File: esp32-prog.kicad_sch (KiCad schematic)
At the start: 43 parts, among them J1 USB_B_Micro_10118194-0001LF, J2 1.27mm_50mils_male_DW127R-22-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, Q1 AO3400A, Q2 AO3400A, SW1 SW_DIP_x02_50mil_1.27mm_TP-02, U1 AMS1117-3.3, U2 SRV05-4, U3 CH340C, U4 74LVC1G125GW_Nexperia, U5 74LVC1G125GW_Nexperia, U6 74LVC1G125GW_Nexperia, U7 74LVC1G125GW_Nexperia

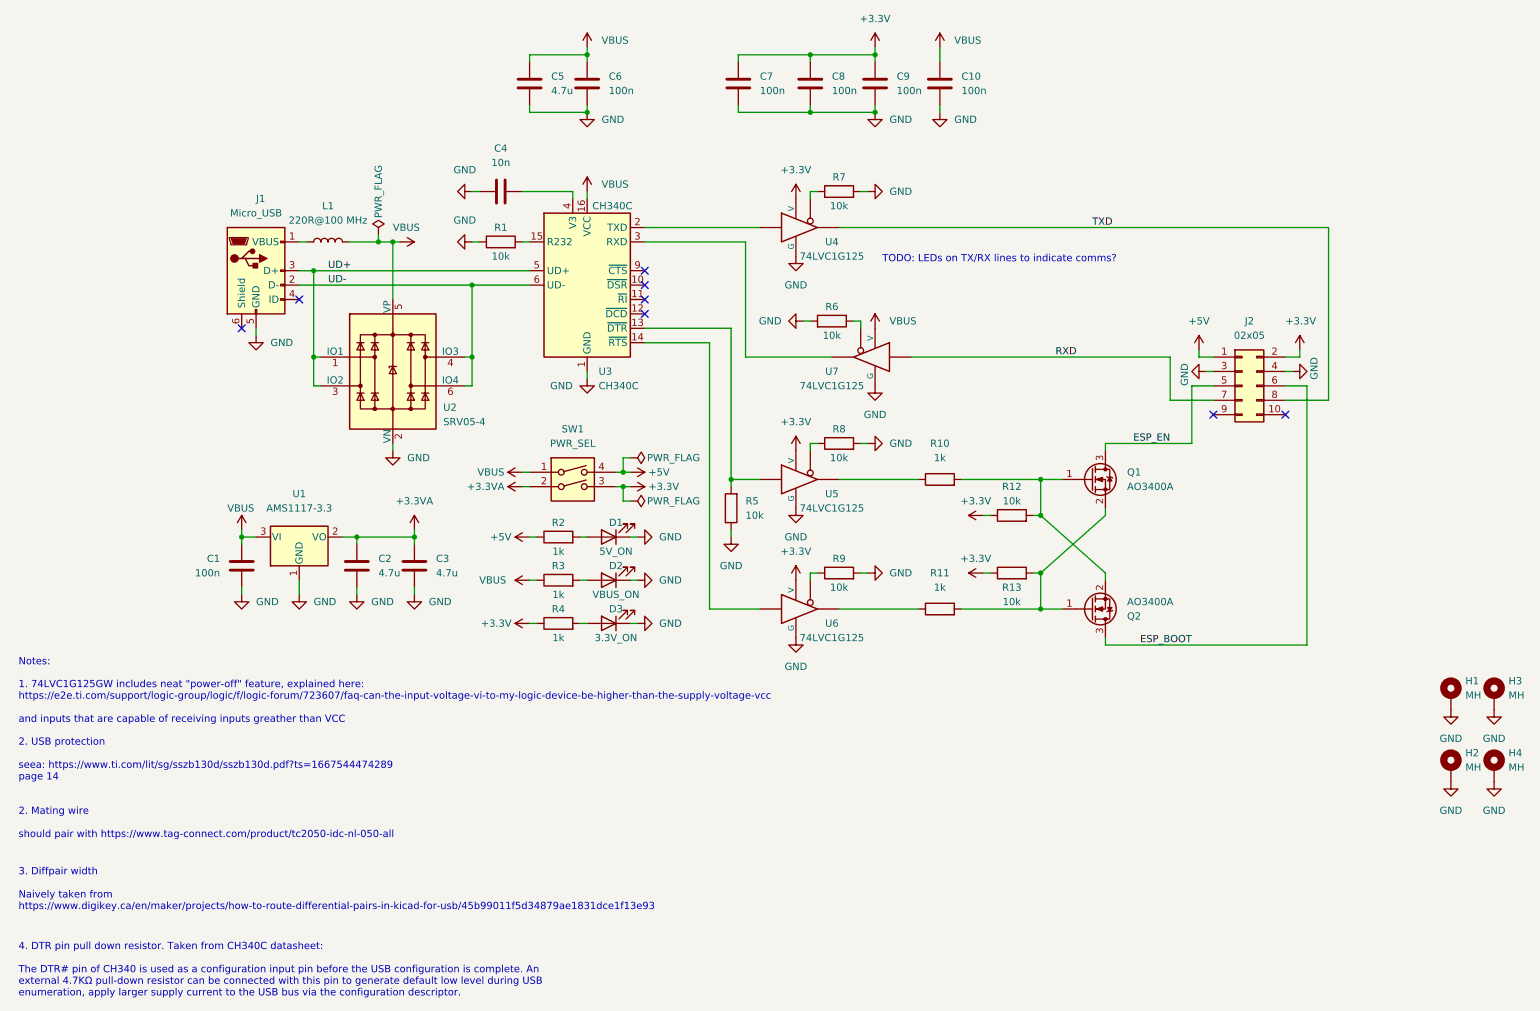
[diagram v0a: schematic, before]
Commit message: pcb: next revision schematics and prelim routing
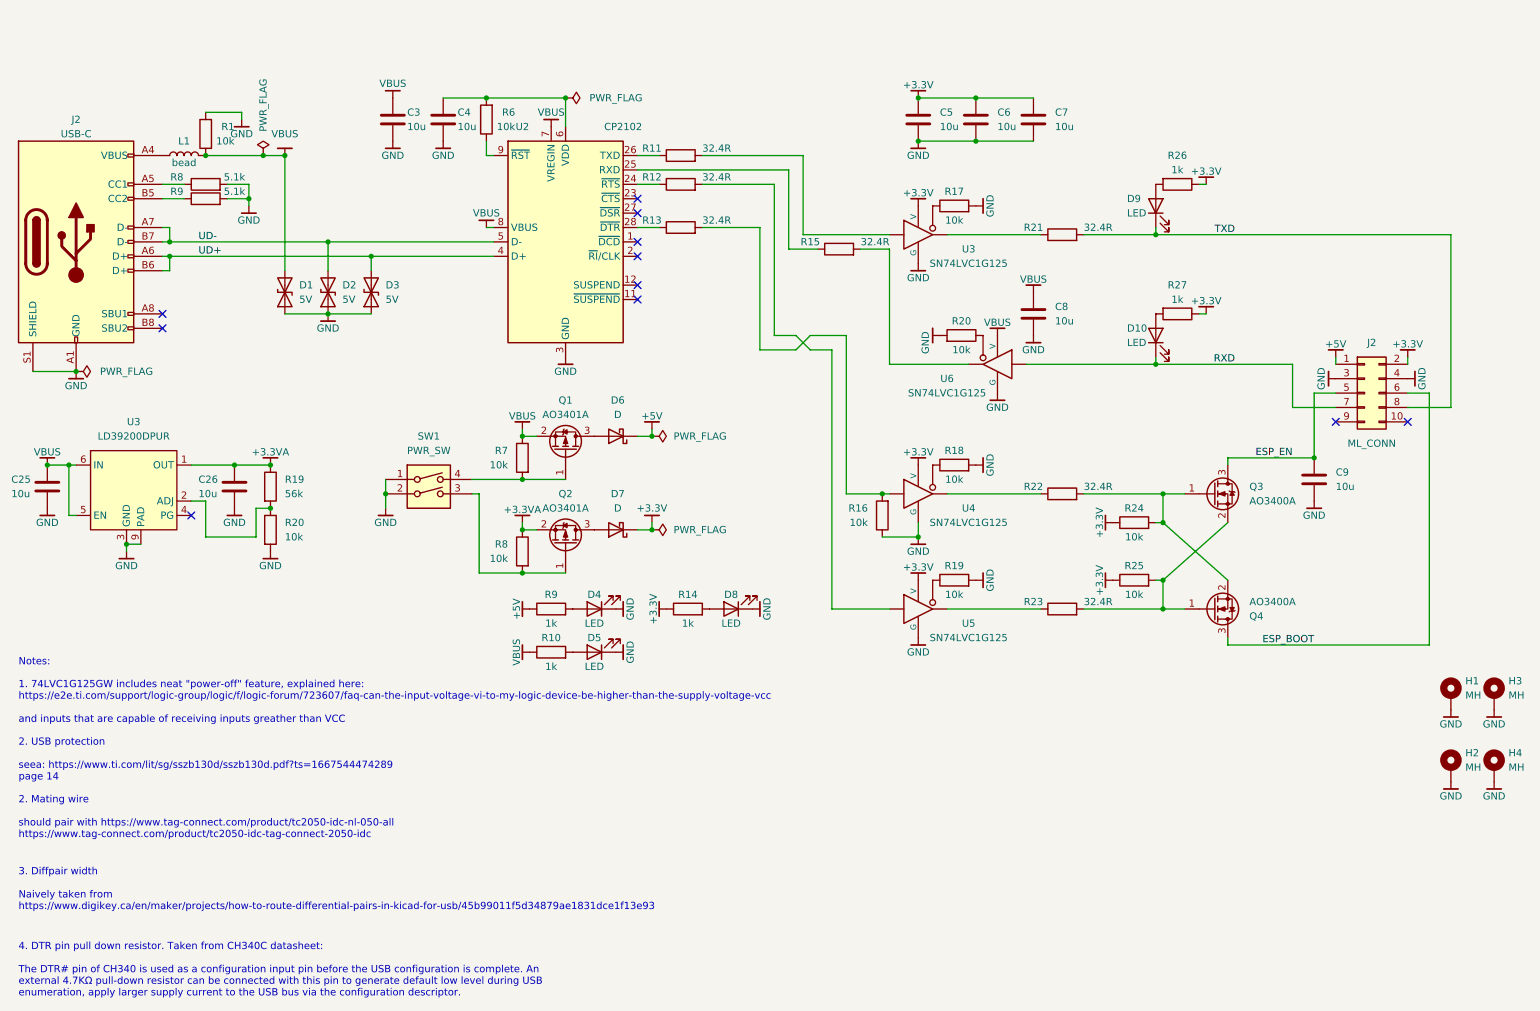
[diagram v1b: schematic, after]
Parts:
- removed C1, C6: 100n_0402_CL05B104KB54PNC, Capacitor_SMD:C_0603_1608Metric, symbol 00-kiml-capacitors-smd:100n_0402_CL05B104KB54PNC
- removed C2, C3, C5: 4.7u_1206_1206B475K500NT, Capacitor_SMD:C_1206_3216Metric, symbol 00-kiml-capacitors-smd:4.7u_1206_1206B475K500NT
- removed C4: 10n_0402_CL05B103KB5NNNC, Capacitor_SMD:C_0603_1608Metric, symbol 00-kiml-capacitors-smd:10n_0402_CL05B103KB5NNNC
- removed J1: USB_B_Micro_10118194-0001LF, 00-kiml-connector-usb:USB_Micro-B_Amphenol_10118194_Horizontal, symbol 00-kiml-connector:USB_B_Micro_10118194-0001LF
- removed J2: 1.27mm_50mils_male_DW127R-22-10-23_02x05, Connector_PinHeader_1.27mm:PinHeader_2x05_P1.27mm_Vertical, symbol 00-kiml-connector-pin-header-1.27mm:1.27mm_50mils_male_DW127R-22-10-23_02x05
- removed L1: 0805_FB_220R@100MHz_BLM21PG221SN1D, Inductor_SMD:L_0805_2012Metric_Pad1.15x1.40mm_HandSolder, symbol 00-kiml-inductors:0805_FB_220R@100MHz_BLM21PG221SN1D
- removed R10, R11: 1k_0402_0402WGF1001TCE, Resistor_SMD:R_0402_1005Metric, symbol 00-kiml-resistors-smd:1k_0402_0402WGF1001TCE
- removed U1: AMS1117-3.3, Package_TO_SOT_SMD:SOT-223-3_TabPin2, symbol 00-kiml-regulator-linear:AMS1117-3.3
- removed U2: SRV05-4, Package_TO_SOT_SMD:SOT-23-6, symbol 00-kiml-power-protection:SRV05-4
- removed U3: CH340C, Package_SO:SOIC-16_3.9x9.9mm_P1.27mm, symbol 00-kiml-interface_usb:CH340C
- removed U4, U5, U6, U7: 74LVC1G125GW_Nexperia, Package_TO_SOT_SMD:SOT-353_SC-70-5, symbol 00-kiml-74xGxx:74LVC1G125GW_Nexperia
- added C25, C26, C3, C4, C9: 10u_0402_LDK105CBJ106MVLF, Capacitor_SMD:C_0402_1005Metric, symbol 00-kiml-capacitors-smd:10u_0402_LDK105CBJ106MVLF
- added D1, D2, D3: SOD-882_0402_RCLAMP0521P-N, Diode_SMD:D_0402_1005Metric, symbol 00-kiml-power-protection:SOD-882_0402_RCLAMP0521P-N
- added D10, D9: 0402_BLUE_NCD0402B1, LED_SMD:LED_0402_1005Metric, symbol 00-kiml-led-smd:0402_BLUE_NCD0402B1
- added D6, D7: SS34, 00-kiml-diode:DO-214AC, symbol 00-kiml-diode:SS34
- added J2: TYPE-C-31-M-12, 00-kiml-connector-usb:USB_C_Receptacle_HRO_TYPE-C-31-M-12, symbol 00-kiml-connector-usb:USB_C_Receptacle_USB2.0_TYPE-C-31-M-12
- added J2: Conn-02x05_PZ254-2-05-Z-8.5, Connector_PinHeader_2.54mm:PinHeader_2x05_P2.54mm_Vertical, symbol 00-kiml-connector-pin-header-2.54mm:Conn-02x05_PZ254-2-05-Z-8.5
- added L1: FB_2A_0805_220R@100MHz_BLM21PG221SN1D, Inductor_SMD:L_0805_2012Metric_Pad1.15x1.40mm_HandSolder, symbol 00-kiml-inductors:FB_2A_0805_220R@100MHz_BLM21PG221SN1D
- added Q1, Q2: AO3401A, Package_TO_SOT_SMD:SOT-23, symbol 00-kiml-transistor-fet:AO3401A
- added R11, R12, R13, R15, R21, R22, R23: 32.4R_0402_AC0402FR-0732R4L, Resistor_SMD:R_0402_1005Metric, symbol 00-kiml-resistors-smd:32.4R_0402_AC0402FR-0732R4L
- added R19: 56k_0402_ERJ2RKF5602X, Resistor_SMD:R_0402_1005Metric, symbol 00-kiml-resistors-smd:56k_0402_ERJ2RKF5602X
- added R20, R6, R7, R8: 10k_0402_0402WGF1002TCE, Resistor_SMD:R_0402_1005Metric, symbol 00-kiml-resistors-smd:10k_0402_0402WGF1002TCE
- added R26, R27: 1k_0402_0402WGF1001TCE, Resistor_SMD:R_0402_1005Metric, symbol 00-kiml-resistors-smd:1k_0402_0402WGF1001TCE
- added R8, R9: 5.1k_0603_0603WAF5101T5E, Resistor_SMD:R_0603_1608Metric, symbol 00-kiml-resistors-smd:5.1k_0603_0603WAF5101T5E
- added U2: CP2102-GMR, Package_DFN_QFN:QFN-28-1EP_5x5mm_P0.5mm_EP3.35x3.35mm, symbol 00-kiml-interface_usb:CP2102-GMR
- added U3: LD39200DPUR, Package_DFN_QFN:DFN-8-1EP_4x4mm_P0.8mm_EP2.3x3.24mm, symbol 00-kiml-regulator-linear:LD39200DPUR
- added U3, U4, U5, U6: TI_SN74LVC1G125DRYR, Package_SON:Texas_USON-6_1x1.45mm_P0.5mm_SMD, symbol 00-kiml-74xGxx:TI_SN74LVC1G125DRYR
- C5: renamed from C7; value 100n_0402_CL05B104KB54PNC -> 10u_0402_LDK105CBJ106MVLF; footprint Capacitor_SMD:C_0603_1608Metric -> Capacitor_SMD:C_0402_1005Metric; symbol 00-kiml-capacitors-smd:100n_0402_CL05B104KB54PNC -> 00-kiml-capacitors-smd:10u_0402_LDK105CBJ106MVLF; LNK1 https://jlcpcb.com/partdetail/291005-CL05B104KB54PNC/C307331 -> https://jlcpcb.com/partdetail/TaiyoYuden-LDK105CBJ106MVLF/C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; MFR Samsung -> Taiyo; MPN CL05B104KB54PNC -> LDK105CBJ106MVLF; Rating 50V -> 10V; SNB1 Basic part -> Extended Part; SPN1 C307331 -> C386033; Tolerance 10% -> (none); UserValue 100n -> 10u
- C6: renamed from C8; value 100n_0402_CL05B104KB54PNC -> 10u_0402_LDK105CBJ106MVLF; footprint Capacitor_SMD:C_0603_1608Metric -> Capacitor_SMD:C_0402_1005Metric; symbol 00-kiml-capacitors-smd:100n_0402_CL05B104KB54PNC -> 00-kiml-capacitors-smd:10u_0402_LDK105CBJ106MVLF; LNK1 https://jlcpcb.com/partdetail/291005-CL05B104KB54PNC/C307331 -> https://jlcpcb.com/partdetail/TaiyoYuden-LDK105CBJ106MVLF/C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; MFR Samsung -> Taiyo; MPN CL05B104KB54PNC -> LDK105CBJ106MVLF; Rating 50V -> 10V; SNB1 Basic part -> Extended Part; SPN1 C307331 -> C386033; Tolerance 10% -> (none); UserValue 100n -> 10u
- C7: renamed from C9; value 100n_0402_CL05B104KB54PNC -> 10u_0402_LDK105CBJ106MVLF; footprint Capacitor_SMD:C_0603_1608Metric -> Capacitor_SMD:C_0402_1005Metric; symbol 00-kiml-capacitors-smd:100n_0402_CL05B104KB54PNC -> 00-kiml-capacitors-smd:10u_0402_LDK105CBJ106MVLF; LNK1 https://jlcpcb.com/partdetail/291005-CL05B104KB54PNC/C307331 -> https://jlcpcb.com/partdetail/TaiyoYuden-LDK105CBJ106MVLF/C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; MFR Samsung -> Taiyo; MPN CL05B104KB54PNC -> LDK105CBJ106MVLF; Rating 50V -> 10V; SNB1 Basic part -> Extended Part; SPN1 C307331 -> C386033; Tolerance 10% -> (none); UserValue 100n -> 10u
- C8: renamed from C10; value 100n_0402_CL05B104KB54PNC -> 10u_0402_LDK105CBJ106MVLF; footprint Capacitor_SMD:C_0603_1608Metric -> Capacitor_SMD:C_0402_1005Metric; symbol 00-kiml-capacitors-smd:100n_0402_CL05B104KB54PNC -> 00-kiml-capacitors-smd:10u_0402_LDK105CBJ106MVLF; LNK1 https://jlcpcb.com/partdetail/291005-CL05B104KB54PNC/C307331 -> https://jlcpcb.com/partdetail/TaiyoYuden-LDK105CBJ106MVLF/C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; MFR Samsung -> Taiyo; MPN CL05B104KB54PNC -> LDK105CBJ106MVLF; Rating 50V -> 10V; SNB1 Basic part -> Extended Part; SPN1 C307331 -> C386033; Tolerance 10% -> (none); UserValue 100n -> 10u
- D4: renamed from D1; value 0603_RED_KT-0603R -> 0402_RED_16-213SDRC/S530-A3/TR8; footprint LED_SMD:LED_0603_1608Metric -> LED_SMD:LED_0402_1005Metric; symbol 00-kiml-led-smd:0603_RED_KT-0603R -> 00-kiml-led-smd:0402_RED_16-213SDRC/S530-A3/TR8; LNK1 https://jlcpcb.com/partdetail/Hubei_KentoElec-KT0603R/C2286 -> https://jlcpcb.com/partdetail/EverlightElec-16_213SDRC_S530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; MFR Hubei KENTO -> Everlight; MPN KT-0603R -> 16-213SDRC/S530-A3/TR8; SNB1 Basic part -> (none); SPN1 C2286 -> C71911; UserValue 5V_ON -> LED
- D5: renamed from D2; value 0603_RED_KT-0603R -> 0402_RED_16-213SDRC/S530-A3/TR8; footprint LED_SMD:LED_0603_1608Metric -> LED_SMD:LED_0402_1005Metric; symbol 00-kiml-led-smd:0603_RED_KT-0603R -> 00-kiml-led-smd:0402_RED_16-213SDRC/S530-A3/TR8; LNK1 https://jlcpcb.com/partdetail/Hubei_KentoElec-KT0603R/C2286 -> https://jlcpcb.com/partdetail/EverlightElec-16_213SDRC_S530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; MFR Hubei KENTO -> Everlight; MPN KT-0603R -> 16-213SDRC/S530-A3/TR8; SNB1 Basic part -> (none); SPN1 C2286 -> C71911; UserValue VBUS_ON -> LED
- D8: renamed from D3; value 0603_RED_KT-0603R -> 0402_RED_16-213SDRC/S530-A3/TR8; footprint LED_SMD:LED_0603_1608Metric -> LED_SMD:LED_0402_1005Metric; symbol 00-kiml-led-smd:0603_RED_KT-0603R -> 00-kiml-led-smd:0402_RED_16-213SDRC/S530-A3/TR8; LNK1 https://jlcpcb.com/partdetail/Hubei_KentoElec-KT0603R/C2286 -> https://jlcpcb.com/partdetail/EverlightElec-16_213SDRC_S530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; MFR Hubei KENTO -> Everlight; MPN KT-0603R -> 16-213SDRC/S530-A3/TR8; SNB1 Basic part -> (none); SPN1 C2286 -> C71911; UserValue 3.3V_ON -> LED
- Q3: renamed from Q1; symbol 00-kiml-transitor-fet:AO3400A -> 00-kiml-transistor-fet:AO3400A
- Q4: renamed from Q2; symbol 00-kiml-transitor-fet:AO3400A -> 00-kiml-transistor-fet:AO3400A
- SW1: footprint 00-kiml-button-switch-smd:SW_DIP_1.27mm_0.50mil_TP-02 -> 00-kiml-switch-button-smd:SW_DIP_1.27mm_0.50mil_TP-02; symbol 00-kiml-button-switch-smd:SW_DIP_x02_50mil_1.27mm_TP-02 -> 00-kiml-switch-button-smd:SW_DIP_x02_50mil_1.27mm_TP-02; UserValue PWR_SEL -> PWR_SW
- renumbered R3 to R10, R4 to R14, R5 to R16, R7 to R17, R8 to R18, R9 to R19, R6 to R20, R12 to R24, R13 to R25, R2 to R9
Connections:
- net +3.3V: now also D7.K, J2.2 (Pin_2), R26.1, R27.1, U3.6 (V), U4.6 (V), U5.6 (V); no longer SW1.3
- net +3.3VA: now also C26.2, Q2.2 (S), R19.1, R8.1, U3.1 (OUT); no longer SW1.2
- net +5V: now also D6.K, J2.1 (Pin_1); no longer SW1.4
- net ESP_BOOT: now also J2.6 (Pin_6)
- net ESP_EN: now also C9.1, J2.5 (Pin_5)
- net GND: now also R1.2, SW1.1, SW1.2, C25.1, C26.1, C3.2, C4.2, C9.2, D1.1 (A1), D2.1 (A1), D3.1 (A1), J2.3 (Pin_3), J2.4 (Pin_4), J2.A1 (GND), J2.A12 (GND), J2.B1 (GND), J2.B12 (GND), J2.S1 (SHIELD), R20.2, R8.2, R9.2, U2.29 (GND), U2.3 (GND), U3.3 (G), U3.3 (GND), U3.9 (PAD), U4.3 (G), U5.3 (G), U6.3 (G); no longer R1.1
- net RXD: now also D10.1 (K), J2.7 (Pin_7), U6.2
- net TXD: now also D9.1 (K), J2.8 (Pin_8), R21.2
- net UD+: now also D3.2 (A2), J2.A6 (D+), J2.B6 (D+), U2.4 (D+)
- net UD-: now also D2.2 (A2), J2.A7 (D-), J2.B7 (D-), U2.5 (D-)
- net VBUS: now also R1.1, C25.2, C3.1, D1.2 (A2), L1.2, Q1.2 (S), R7.1, U2.7 (VREGIN), U2.8 (VBUS), U3.5 (EN), U3.6 (IN), U6.6 (V); no longer SW1.1
- net at R17.1: now also U3.1
- net at Q3.2 (S), Q4.1 (G), R25.2: now also R23.2
- net at Q3.1 (G), Q4.2 (S), R24.2: now also R22.2
- net at R20.1: now also U6.1
- net at R19.1: now also U5.1
- net at R18.1: now also U4.1
- net at R16.2: now also R13.2, U4.2
- new net: R19.2, R20.1, U3.2 (ADJ)
- new net: J2.A5 (CC1), R8.1
- new net: D10.2 (A), R27.2
- new net: R15.2, U6.4
- new net: Q1.1 (G), R7.2, SW1.4
- new net: R22.1, U4.4
- new net: R12.1, U2.24 (~{RTS})
- new net: R15.1, U2.25 (RXD)
- new net: R11.1, U2.26 (TXD)
- new net: R13.1, U2.28 (~{DTR})
- new net: C4.1, R6.2, U2.6 (VDD)
- new net: R6.1, U2.9 (~{RST})
- new net: D7.A, Q2.3 (D)
- new net: J2.A4 (VBUS), J2.A9 (VBUS), J2.B4 (VBUS), J2.B9 (VBUS), L1.1
- new net: J2.B5 (CC2), R9.1
- new net: R21.1, U3.4
- new net: D6.A, Q1.3 (D)
- new net: R12.2, U5.2
- new net: R11.2, U3.2
- new net: D9.2 (A), R26.2
- new net: R23.1, U5.4
- new net: Q2.1 (G), R8.2, SW1.3
- no-connect marks 8 -> 11
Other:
- note added: "2. Mating wire should pair with https://www.tag-connect.com/product/tc2050-idc-nl-050-all https://www.tag-connect.com/product/tc2050-idc-tag-connect-2050-idc"
- note removed: "2. Mating wire should pair with https://www.tag-connect.com/product/tc2050-idc-nl-050-all"
- note removed: "TODO: LEDs on TX/RX lines to indicate comms?"
- moved on the sheet: C5, C6, C7, C8, D4, D5, D8, Q3, Q4, R10, R14, R16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

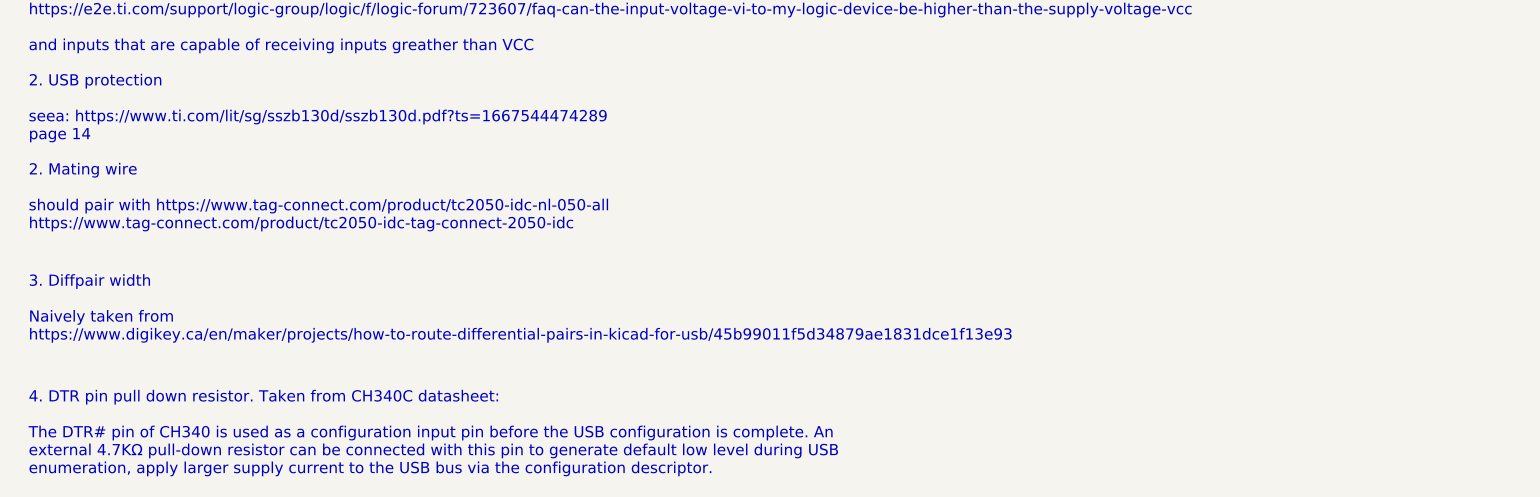
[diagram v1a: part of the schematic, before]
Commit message: pcb: add markings for the tag connector and pwr switch
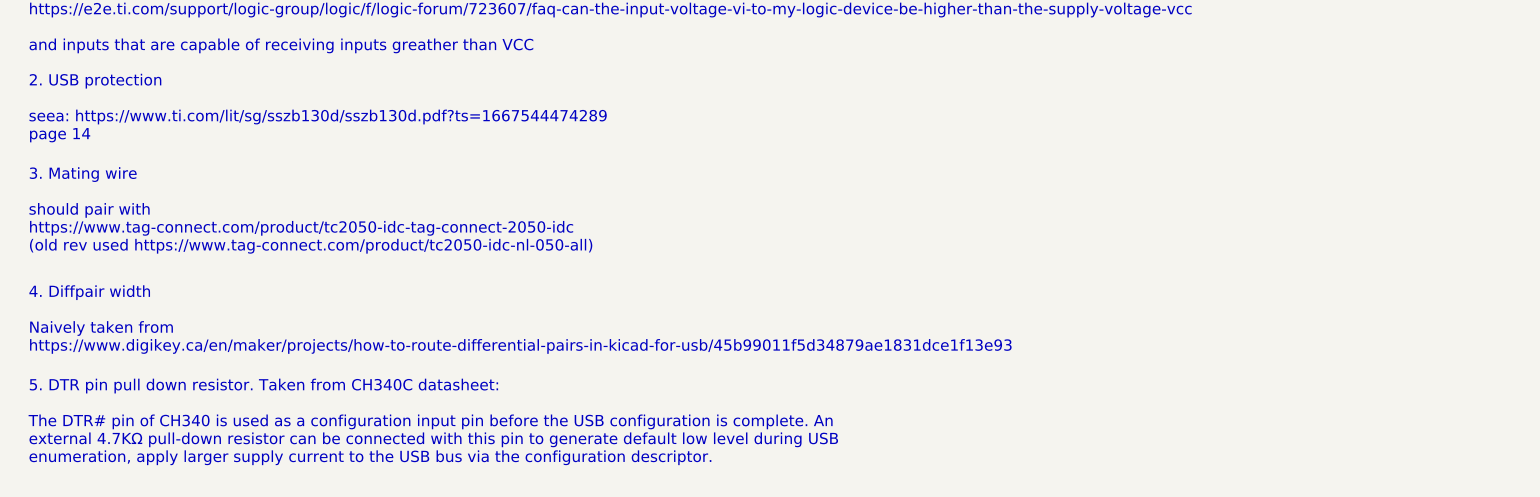
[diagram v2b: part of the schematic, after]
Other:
- note added: "3. Mating wire should pair with https://www.tag-connect.com/product/tc2050-idc-tag-connect-2050-idc (old rev used https://www.tag-connect.com/product/tc2050-idc-nl-050-all)"
- note added: "4. Diffpair width Naively taken from https://www.digikey.ca/en/maker/projects/how-to-route-differential-pairs-in-kicad-for-usb/45b99011f5d34879ae1831dce1f13e93"
- note added: "5. DTR pin pull down resistor. Taken from CH340C datasheet: The DTR# pin of CH340 is used as a configuration input pin before the USB configuration is complete. An external 4.7KΩ pull-down resistor can be connected with this pin to generate default low level during USB enumeration, apply larger supply current to the USB bus via the configuration descriptor."
- note removed: "2. Mating wire should pair with https://www.tag-connect.com/product/tc2050-idc-nl-050-all https://www.tag-connect.com/product/tc2050-idc-tag-connect-2050-idc"
- note removed: "3. Diffpair width Naively taken from https://www.digikey.ca/en/maker/projects/how-to-route-differential-pairs-in-kicad-for-usb/45b99011f5d34879ae1831dce1f13e93"
- note removed: "4. DTR pin pull down resistor. Taken from CH340C datasheet: The DTR# pin of CH340 is used as a configuration input pin before the USB configuration is complete. An external 4.7KΩ pull-down resistor can be connected with this pin to generate default low level during USB enumeration, apply larger supply current to the USB bus via the configuration descriptor."
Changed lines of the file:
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@@
     (stroke (width 0) (type default))
   )
-  (text "4. DTR pin pull down resistor. Taken from CH340C datasheet:\n\nThe DTR# pin of CH340 is used as a configuration input pin before the USB configuration is complete. An\nexternal 4.7KΩ pull-down resistor can be connected with this pin to generate default low level during USB\nenumeration, apply larger supply current to the USB bus via the configuration descriptor."
-    (at 16.51 195.58 0)
+  (text "5. DTR pin pull down resistor. Taken from CH340C datasheet:\n\nThe DTR# pin of CH340 is used as a configuration input pin before the USB configuration is complete. An\nexternal 4.7KΩ pull-down resistor can be connected with this pin to generate default low level during USB\nenumeration, apply larger supply current to the USB bus via the configuration descriptor."
+    (at 16.51 194.31 0)
     (effects (font (size 1.27 1.27)) (justify left bottom))
   )
@@
     (effects (font (size 1.27 1.27)) (justify left bottom))
   )
-  (text "3. Diffpair width\n\nNaively taken from \nhttps://www.digikey.ca/en/maker/projects/how-to-route-differential-pairs-in-kicad-for-usb/45b99011f5d34879ae1831dce1f13e93"
-    (at 16.51 180.34 0)
+  (text "4. Diffpair width\n\nNaively taken from \nhttps://www.digikey.ca/en/maker/projects/how-to-route-differential-pairs-in-kicad-for-usb/45b99011f5d34879ae1831dce1f13e93"
+    (at 16.51 181.61 0)
     (effects (font (size 1.27 1.27)) (justify left bottom))
   )
@@
     (effects (font (size 1.27 1.27)) (justify left bottom))
   )
-  (text "2. Mating wire\n\nshould pair with https://www.tag-connect.com/product/tc2050-idc-nl-050-all\nhttps://www.tag-connect.com/product/tc2050-idc-tag-connect-2050-idc"
-    (at 16.51 167.64 0)
+  (text "3. Mating wire\n\nshould pair with \nhttps://www.tag-connect.com/product/tc2050-idc-tag-connect-2050-idc\n(old rev used https://www.tag-connect.com/product/tc2050-idc-nl-050-all)"
+    (at 16.51 170.18 0)
     (effects (font (size 1.27 1.27)) (justify left bottom))
   )
